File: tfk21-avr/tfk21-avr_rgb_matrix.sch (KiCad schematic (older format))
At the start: 34 parts, among them U2 IS31FL3733-TQ

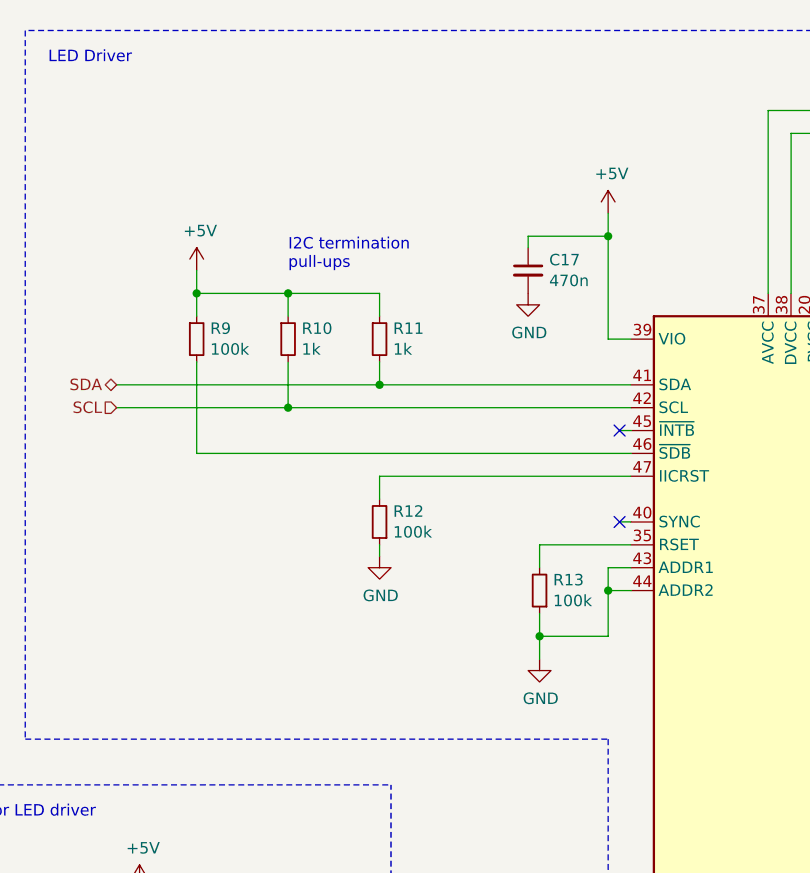
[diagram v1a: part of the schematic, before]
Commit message: Fix LED driver resistors and mounting hole pads
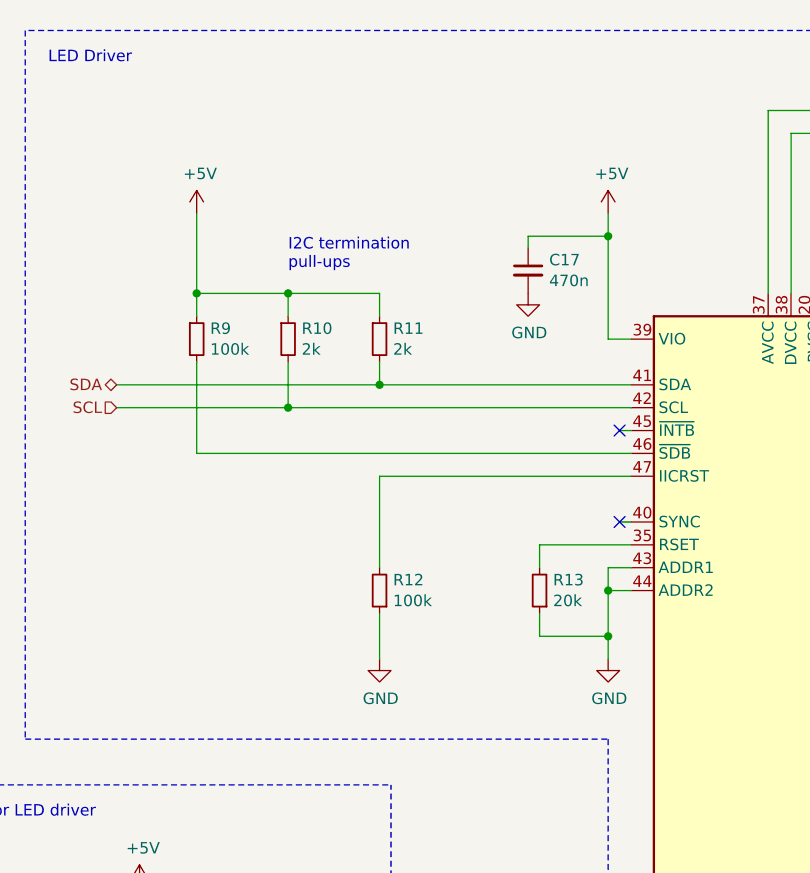
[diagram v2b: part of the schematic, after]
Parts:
- R10, R11: value 1k -> 2k
- R13: value 100k -> 20k
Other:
- moved on the sheet: R12
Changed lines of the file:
@@
 	9250 2550 8150 2550
 Wire Wire Line
-	8150 2550 8150 2650
+	8150 2550 8150 2950
 $Comp
 L Device:R_Small R12
 U 1 1 6021C88C
-P 8150 2750
-F 0 "R12" H 8091 2704 50  0000 R CNN
-F 1 "100k" H 8091 2795 50  0000 R CNN
-F 2 "Resistor_SMD:R_0805_2012Metric_Pad1.20x1.40mm_HandSolder" H 8150 2750 50  0001 C CNN
-F 3 "~" H 8150 2750 50  0001 C CNN
-	1    8150 2750
+P 8150 3050
+F 0 "R12" H 8091 3004 50  0000 R CNN
+F 1 "100k" H 8091 3095 50  0000 R CNN
+F 2 "Resistor_SMD:R_0805_2012Metric_Pad1.20x1.40mm_HandSolder" H 8150 3050 50  0001 C CNN
+F 3 "~" H 8150 3050 50  0001 C CNN
+	1    8150 3050
 	-1   0    0    1
 $EndComp
 Wire Wire Line
-	8150 2850 8150 2900
+	8150 3150 8150 3350
 $Comp
 L power:GND #PWR042
 U 1 1 6021F1B8
-P 8150 2900
-F 0 "#PWR042" H 8150 2650 50  0001 C CNN
-F 1 "GND" H 8155 2727 50  0000 C CNN
-F 2 "" H 8150 2900 50  0001 C CNN
-F 3 "" H 8150 2900 50  0001 C CNN
-	1    8150 2900
+P 8150 3350
+F 0 "#PWR042" H 8150 3100 50  0001 C CNN
+F 1 "GND" H 8155 3177 50  0000 C CNN
+F 2 "" H 8150 3350 50  0001 C CNN
+F 3 "" H 8150 3350 50  0001 C CNN
+	1    8150 3350
 	1    0    0    -1
 $EndComp
@@
 P 7750 1950
 F 0 "R10" H 7809 1996 50  0000 L CNN
-F 1 "1k" H 7809 1905 50  0000 L CNN
+F 1 "2k" H 7809 1905 50  0000 L CNN
 F 2 "Resistor_SMD:R_0805_2012Metric_Pad1.20x1.40mm_HandSolder" H 7750 1950 50  0001 C CNN
 F 3 "~" H 7750 1950 50  0001 C CNN
@@
 P 8150 1950
 F 0 "R11" H 8209 1996 50  0000 L CNN
-F 1 "1k" H 8209 1905 50  0000 L CNN
+F 1 "2k" H 8209 1905 50  0000 L CNN
 F 2 "Resistor_SMD:R_0805_2012Metric_Pad1.20x1.40mm_HandSolder" H 8150 1950 50  0001 C CNN
 F 3 "~" H 8150 1950 50  0001 C CNN
@@
 Connection ~ 7750 1750
 Wire Wire Line
-	7350 1750 7350 1650
+	7350 1750 7350 1400
 Connection ~ 7350 1750
 Text HLabel 7000 2150 0    50   BiDi ~ 0
@@
 P 8850 3050
 F 0 "R13" H 8791 3004 50  0000 R CNN
-F 1 "100k" H 8791 3095 50  0000 R CNN
+F 1 "20k" H 8791 3095 50  0000 R CNN
 F 2 "Resistor_SMD:R_0805_2012Metric_Pad1.20x1.40mm_HandSolder" H 8850 3050 50  0001 C CNN
 F 3 "~" H 8850 3050 50  0001 C CNN
@@
 	8850 3250 8850 3150
 Connection ~ 9150 3050
-Connection ~ 8850 3250
-Wire Wire Line
-	8850 3250 8850 3350
+Wire Wire Line
+	9150 3250 9150 3350
 $Comp
 L power:GND #PWR043
 U 1 1 6022B57B
-P 8850 3350
-F 0 "#PWR043" H 8850 3100 50  0001 C CNN
-F 1 "GND" H 8855 3177 50  0000 C CNN
-F 2 "" H 8850 3350 50  0001 C CNN
-F 3 "" H 8850 3350 50  0001 C CNN
-	1    8850 3350
+P 9150 3350
+F 0 "#PWR043" H 9150 3100 50  0001 C CNN
+F 1 "GND" H 9155 3177 50  0000 C CNN
+F 2 "" H 9150 3350 50  0001 C CNN
+F 3 "" H 9150 3350 50  0001 C CNN
+	1    9150 3350
 	1    0    0    -1
 $EndComp
@@
 L power:+5V #PWR040
 U 1 1 613849FC
-P 7350 1650
-F 0 "#PWR040" H 7350 1500 50  0001 C CNN
-F 1 "+5V" H 7365 1823 50  0000 C CNN
-F 2 "" H 7350 1650 50  0001 C CNN
-F 3 "" H 7350 1650 50  0001 C CNN
-	1    7350 1650
+P 7350 1400
+F 0 "#PWR040" H 7350 1250 50  0001 C CNN
+F 1 "+5V" H 7365 1573 50  0000 C CNN
+F 2 "" H 7350 1400 50  0001 C CNN
+F 3 "" H 7350 1400 50  0001 C CNN
+	1    7350 1400
 	1    0    0    -1
 $EndComp
@@
 Wire Wire Line
 	850  1500 950  1500
+Connection ~ 9150 3250
 $EndSCHEMATC

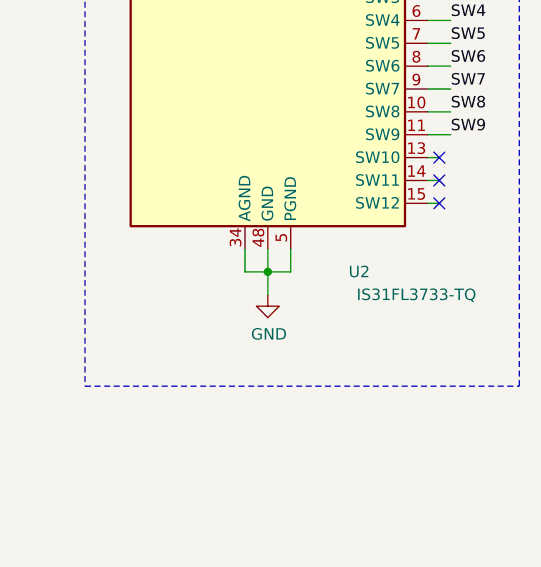
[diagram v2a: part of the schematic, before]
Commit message: Use newer revision of LED driver
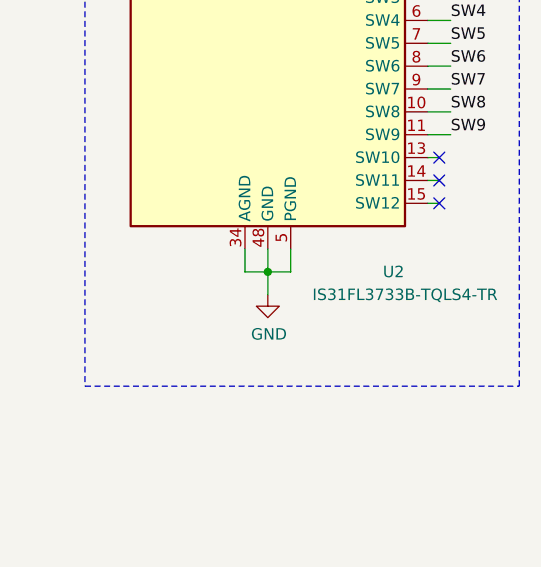
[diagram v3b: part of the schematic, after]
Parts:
- U2: value IS31FL3733-TQ -> IS31FL3733B-TQLS4-TR
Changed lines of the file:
@@
 U 1 1 602119B1
 P 9950 3350
-F 0 "U2" H 10350 1650 50  0000 C CNN
-F 1 "IS31FL3733-TQ" H 10600 1550 50  0000 C CNN
+F 0 "U2" H 10500 1650 50  0000 C CNN
+F 1 "IS31FL3733B-TQLS4-TR" H 10550 1550 50  0000 C CNN
 F 2 "Package_QFP:TQFP-48-1EP_7x7mm_P0.5mm_EP5x5mm_ThermalVias" H 9950 3350 50  0001 C CNN
-F 3 "http://www.issi.com/WW/pdf/IS31FL3733.pdf" H 9950 3350 50  0001 C CNN
+F 3 "https://www.lumissil.com/assets/pdf/core/IS31FL3733B_DS.pdf" H 9950 3350 50  0001 C CNN
 	1    9950 3350
 	1    0    0    -1
